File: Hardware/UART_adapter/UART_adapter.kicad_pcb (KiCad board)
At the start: 2 copper layers, 99.5 x 34.5 mm, 2 parts, among them J2 Conn_02x07_Top_Bottom

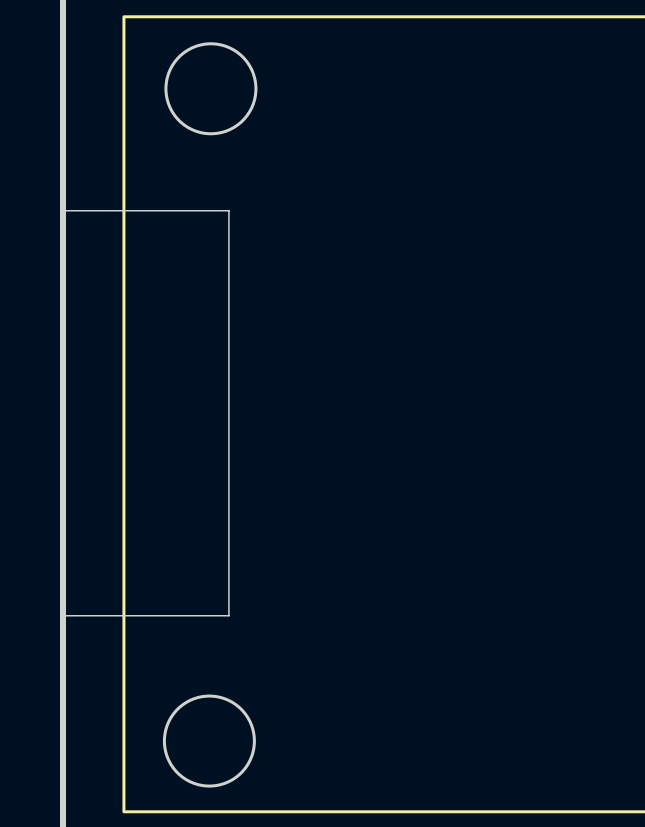
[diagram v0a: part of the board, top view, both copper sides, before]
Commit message: Fixed RF trace, Added new Diodes, better power traces and new switches
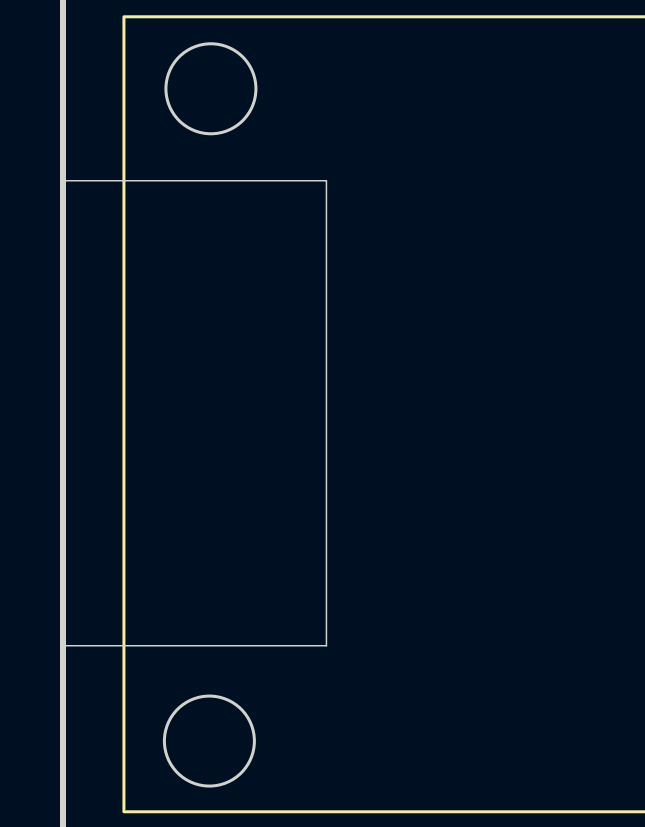
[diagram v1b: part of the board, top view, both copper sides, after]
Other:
- outline, holes or cut-outs redrawn
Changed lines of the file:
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@@
 	)
 	(gr_rect
-		(start 92.9873 94.5158)
-		(end 98.5185 108.0158)
+		(start 92.9873 93.5158)
+		(end 101.7685 109.0158)
 		(stroke
 			(width 0.05)

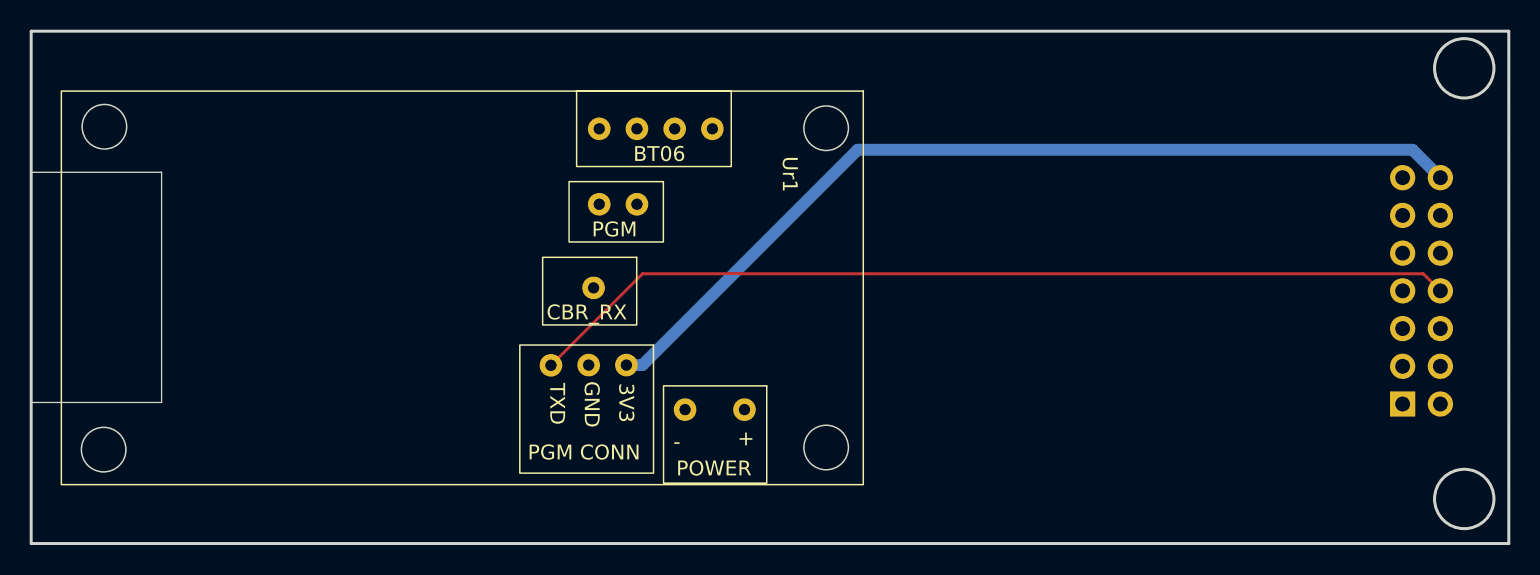
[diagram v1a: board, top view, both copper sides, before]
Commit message: Updated eggfinder to correct wiring
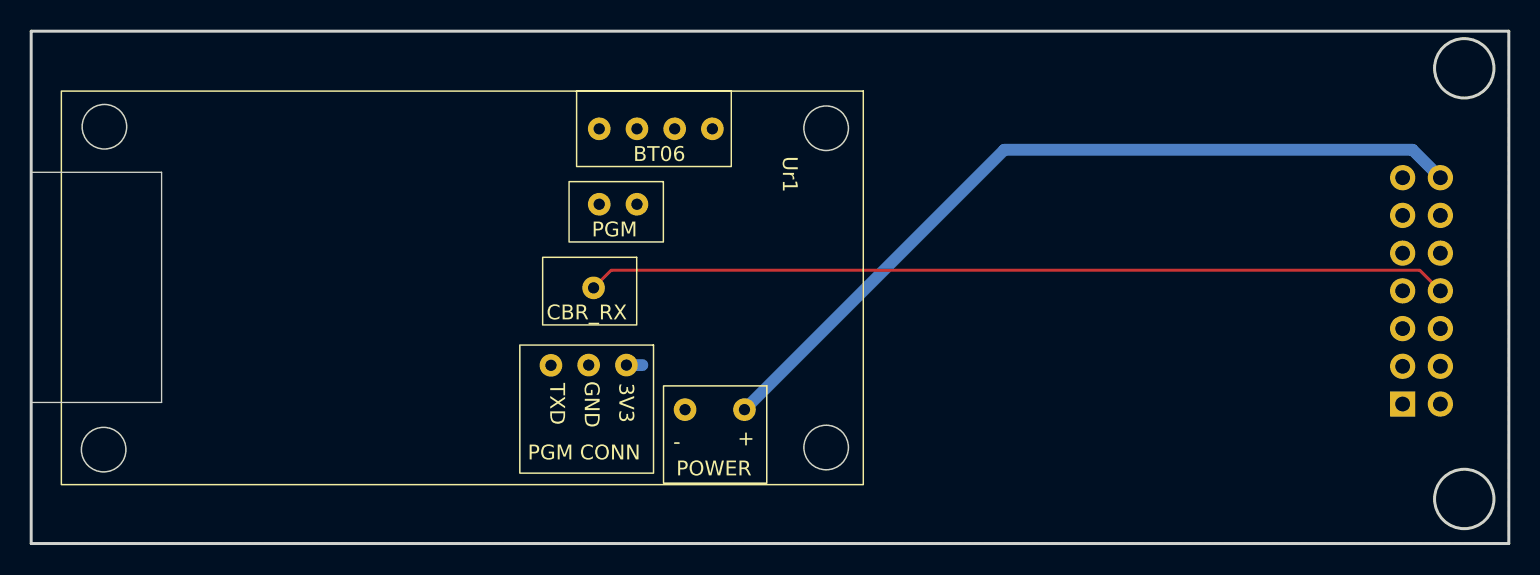
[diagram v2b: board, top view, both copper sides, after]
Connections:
- Ur1 pad 10: /RADIO_RX -> unconnected-(Ur1-PGM_CONN_TXD-Pad10)
- Ur1 pad 12: +3.3V -> unconnected-(Ur1-PGM_CONN_3V3-Pad12)
- Ur1 pad 7: unconnected-(Ur1-CBR_RX-Pad7) -> /RADIO_RX
- Ur1 pad 9: unconnected-(Ur1-5V-Pad9) -> +3.3V
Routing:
- net +3.3V: track 61.6 -> 54.9 mm
- net /RADIO_RX: track 62.9 -> 58.1 mm
- net unconnected-(Ur1-PGM_CONN_3V3-Pad12): track 0.00 -> 1.08 mm
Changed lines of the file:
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@@
 	(net 11 "+3.3V")
 	(net 12 "unconnected-(Ur1-PWM_1-Pad5)")
-	(net 13 "unconnected-(Ur1-5V-Pad9)")
-	(net 14 "unconnected-(Ur1-CBR_RX-Pad7)")
+	(net 13 "unconnected-(Ur1-PGM_CONN_3V3-Pad12)")
+	(net 14 "unconnected-(Ur1-PGM_CONN_TXD-Pad10)")
 	(net 15 "unconnected-(Ur1-BT06_3V3-Pad4)")
 	(net 16 "unconnected-(Ur1-PWM_2-Pad6)")
@@
 			(layers "*.Cu" "*.Mask")
 			(remove_unused_layers no)
-			(net 14 "unconnected-(Ur1-CBR_RX-Pad7)")
+			(net 1 "/RADIO_RX")
 			(pinfunction "CBR_RX")
-			(pintype "input+no_connect")
+			(pintype "input")
 		)
 		(pad "8" thru_hole circle
@@
 			(layers "*.Cu" "*.Mask")
 			(remove_unused_layers no)
-			(net 13 "unconnected-(Ur1-5V-Pad9)")
+			(net 11 "+3.3V")
 			(pinfunction "5V")
-			(pintype "input+no_connect")
+			(pintype "input")
 		)
 		(pad "10" thru_hole circle
@@
 			(layers "*.Cu" "*.Mask")
 			(remove_unused_layers no)
-			(net 1 "/RADIO_RX")
+			(net 14 "unconnected-(Ur1-PGM_CONN_TXD-Pad10)")
 			(pinfunction "PGM_CONN_TXD")
-			(pintype "input")
+			(pintype "input+no_connect")
 		)
 		(pad "11" thru_hole circle
@@
 			(layers "*.Cu" "*.Mask")
 			(remove_unused_layers no)
-			(net 11 "+3.3V")
+			(net 13 "unconnected-(Ur1-PGM_CONN_3V3-Pad12)")
 			(pinfunction "PGM_CONN_3V3")
-			(pintype "input")
+			(pintype "input+no_connect")
 		)
 		(embedded_fonts no)
@@
 	)
 	(segment
-		(start 186.727627 100.350372)
-		(end 134.152728 100.350372)
+		(start 186.489627 100.112372)
+		(end 132.045128 100.112372)
+		(width 0.2)
+		(layer "F.Cu")
+		(net 1)
+	)
+	(segment
+		(start 132.045128 100.112372)
+		(end 130.8575 101.3)
 		(width 0.2)
 		(layer "F.Cu")
@@
 	(segment
 		(start 187.878627 101.501372)
-		(end 186.727627 100.350372)
+		(end 186.489627 100.112372)
 		(width 0.2)
 		(layer "F.Cu")
@@
 	)
 	(segment
-		(start 134.152728 100.350372)
-		(end 127.9873 106.5158)
-		(width 0.2)
-		(layer "F.Cu")
-		(net 1)
+		(start 158.5185 92)
+		(end 141.0185 109.5)
+		(width 0.8)
+		(layer "B.Cu")
+		(net 11)
 	)
 	(segment
-		(start 134.14613 106.5)
-		(end 133.0685 106.5)
+		(start 185.997255 92)
+		(end 158.5185 92)
 		(width 0.8)
 		(layer "B.Cu")
@@
 	)
 	(segment
-		(start 148.64613 92)
-		(end 134.14613 106.5)
+		(start 134.14613 106.5)
+		(end 133.0685 106.5)
 		(width 0.8)
 		(layer "B.Cu")
-		(net 11)
-	)
-	(segment
-		(start 185.997255 92)
-		(end 148.64613 92)
-		(width 0.8)
-		(layer "B.Cu")
-		(net 11)
+		(net 13)
 	)
 	(zone

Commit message: Added HiPR logos and fixed mounting wholes
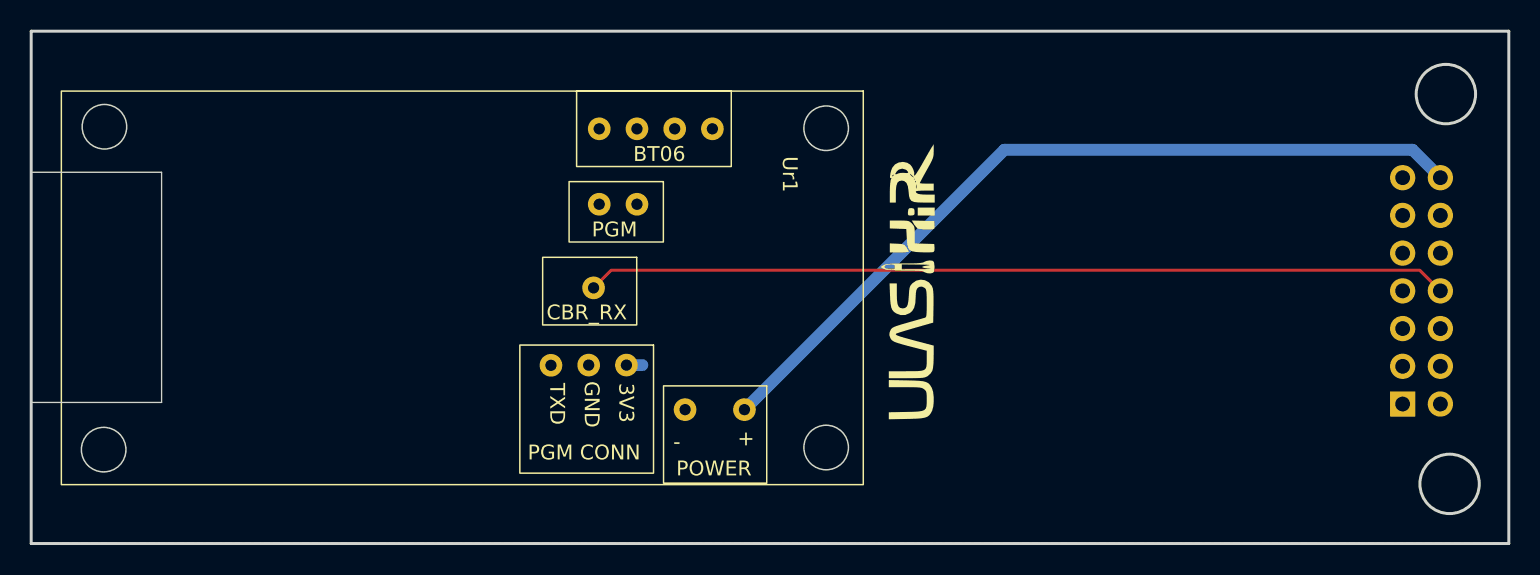
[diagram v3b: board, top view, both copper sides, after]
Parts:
- added G***: LOGO, Eggfinder RX:HiPR, F.Cu at (152.2, 101.0)
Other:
- outline, holes or cut-outs redrawn

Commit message: hardware done
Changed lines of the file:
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@@
 			(drillshape 0)
 			(scaleselection 1)
-			(outputdirectory "../Manufacturing/UART_adapter/Gerber Output/")
+			(outputdirectory "../Manufacturing/UART_adapter/fabrication/")
 		)
 	)
@@
 		(net 6)
 		(net_name "GND")
-		(layer "F.Cu")
+		(layers "F.Cu" "B.Cu")
 		(hatch edge 0.5)
 		(priority 1)
